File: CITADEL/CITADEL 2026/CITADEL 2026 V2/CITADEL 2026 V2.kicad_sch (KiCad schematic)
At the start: 71 parts, among them J1 FAERIE CAN BUS, J10 ESC PWR, J11 STEPPER 1, J12 STEPPER 2, J13 SERVO DAUGHTER, J2 CITADEL CAN BUS, J3 FAERIE 12V, J4 CITADEL BATTERY, J5 FAERIE BATTERY, J6 LED STRIP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

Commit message: Removed stepper drivers
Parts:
- removed A1, A2: DRV8825, Module:Pololu_Breakout-16_15.2x20.3mm, symbol Driver_Motor:Pololu_Breakout_DRV8825
- removed J11: STEPPER 1, Connector_Molex:Molex_Mini-Fit_Jr_5566-04A_2x02_P4.20mm_Vertical, symbol Connector:Conn_01x04_Socket
- removed J12: STEPPER 2, Connector_Molex:Molex_Mini-Fit_Jr_5566-04A_2x02_P4.20mm_Vertical, symbol Connector:Conn_01x04_Socket
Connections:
- net STEPPER1_STEP: no longer names the net of U1.J3_8 (MTDO/GPIO40)
- net STEPPER2_STEP: no longer names the net of U1.J3_10 (GPIO38)
- net STEPPER_DIR: no longer names the net of U1.J3_9 (MTCK/GPIO39)
- net STEPPER_EN: no longer names the net of U1.J3_4 (GPIO1)
- net STEPPER_M0: no longer names the net of U1.J3_5 (GPIO2)
- net STEPPER_M1: no longer names the net of U1.J3_6 (MTMS/GPIO42)
- net STEPPER_M2: no longer names the net of U1.J3_7 (MTDI/GPIO41)
- no-connect marks 35 -> 40
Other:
- moved on the sheet: C4, J6, J7, J8, R14, R15, R16, R17, R18, R19, R20, R21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

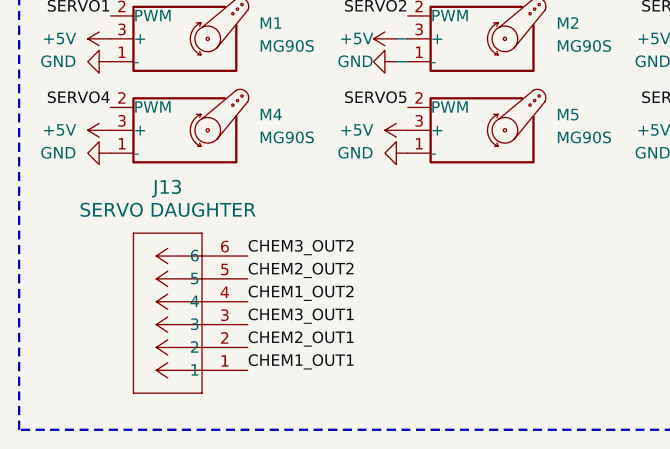
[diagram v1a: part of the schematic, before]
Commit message: Changed linear actuator connectors
Removed the connector for the daughter board and moved the 1x2 molex connectors onto main board
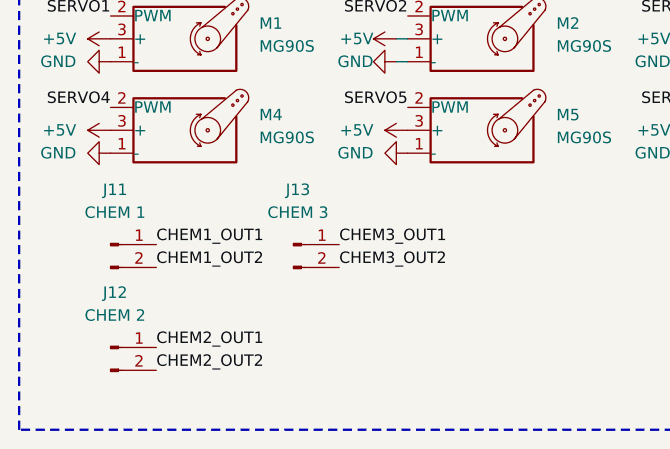
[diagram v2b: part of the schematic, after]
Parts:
- removed J13: SERVO DAUGHTER, Jayse_Footprints:MOLEX_0039281063, symbol 2026-01-24_03-47-07:39281063
- added J11: CHEM 1, Connector_Molex:Molex_Mini-Fit_Jr_5566-02A_2x01_P4.20mm_Vertical, symbol Connector:Conn_01x02_Pin
- added J12: CHEM 2, Connector_Molex:Molex_Mini-Fit_Jr_5566-02A_2x01_P4.20mm_Vertical, symbol Connector:Conn_01x02_Pin
- added J13: CHEM 3, Connector_Molex:Molex_Mini-Fit_Jr_5566-02A_2x01_P4.20mm_Vertical, symbol Connector:Conn_01x02_Pin
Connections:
- net CHEM1_OUT1: now also J11.1 (Pin_1)
- net CHEM1_OUT2: now also J11.2 (Pin_2)
- net CHEM2_OUT1: now also J12.1 (Pin_1)
- net CHEM2_OUT2: now also J12.2 (Pin_2)
- net CHEM3_OUT1: now also J13.1 (Pin_1)
- net CHEM3_OUT2: now also J13.2 (Pin_2)
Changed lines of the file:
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@@
 	)
 	(label "CHEM3_OUT2"
-		(at 43.18 218.44 0)
+		(at 53.34 219.71 0)
 		(effects
 			(font
@@
 	)
 	(label "CHEM3_OUT1"
-		(at 43.18 226.06 0)
+		(at 53.34 217.17 0)
 		(effects
 			(font
@@
 	)
 	(label "CHEM1_OUT2"
-		(at 43.18 223.52 0)
+		(at 33.02 219.71 0)
 		(effects
 			(font
@@
 	)
 	(label "CHEM2_OUT1"
-		(at 43.18 228.6 0)
+		(at 33.02 228.6 0)
 		(effects
 			(font
@@
 	)
 	(label "CHEM1_OUT1"
-		(at 43.18 231.14 0)
+		(at 33.02 217.17 0)
 		(effects
 			(font
@@
 	)
 	(label "CHEM2_OUT2"
-		(at 43.18 220.98 0)
+		(at 33.02 231.14 0)
 		(effects
 			(font
@@
 	)
 	(symbol
+		(lib_id "Connector:Conn_01x02_Pin")
+		(at 27.94 217.17 0)
+		(unit 1)
+		(exclude_from_sim no)
+		(in_bom yes)
+		(on_board yes)
+		(dnp no)
+		(property "Reference" "J11"
+			(at 28.448 211.074 0)
+			(effects
+				(font
+					(size 1.27 1.27)
+				)
+			)
+		)
+		(property "Value" "CHEM 1"
+			(at 28.448 213.614 0)
+			(effects
+				(font
+					(size 1.27 1.27)
+				)
+			)
+		)
+		(property "Footprint" "Connector_Molex:Molex_Mini-Fit_Jr_5566-02A_2x01_P4.20mm_Vertical"
+			(at 27.94 217.17 0)
+			(effects
+				(font
+					(size 1.27 1.27)
+				)
+				(hide yes)
+			)
+		)
+		(property "Datasheet" "~"
+			(at 27.94 217.17 0)
+			(effects
+				(font
+					(size 1.27 1.27)
+				)
+				(hide yes)
+			)
+		)
+		(property "Description" "Generic connector, single row, 01x02, script generated"
+			(at 27.94 217.17 0)
+			(effects
+				(font
+					(size 1.27 1.27)
+				)
+				(hide yes)
+			)
+		)
+		(pin "1"
+		)
+		(pin "2"
+		)
+		(instances
+			(project "CITADEL 2026 V2"
+				(path "/90a2ddca-ec68-4195-87ff-b70a09174bf7"
+					(reference "J11")
+					(unit 1)
+				)
+			)
+		)
+	)
+	(symbol
 		(lib_id "power:GND")
 		(at 93.98 196.85 270)
@@
 	)
 	(symbol
-		(lib_id "2026-01-24_03-47-07:39281063")
-		(at 43.18 231.14 180)
-		(unit 1)
-		(exclude_from_sim no)
-		(in_bom yes)
-		(on_board yes)
-		(dnp no)
-		(fields_autoplaced yes)
-		(property "Reference" "J13"
-			(at 34.29 210.82 0)
-			(effects
-				(font
-					(size 1.524 1.524)
-				)
-			)
-		)
-		(property "Value" "SERVO DAUGHTER"
-			(at 34.29 213.36 0)
-			(effects
-				(font
-					(size 1.524 1.524)
-				)
-			)
-		)
-		(property "Footprint" "Jayse_Footprints:MOLEX_0039281063"
-			(at 43.18 231.14 0)
-			(effects
-				(font
-					(size 1.27 1.27)
-					(italic yes)
-				)
-				(hide yes)
-			)
-		)
-		(property "Datasheet" "https://www.molex.com/en-us/products/part-detail-pdf/39281063?display=pdf"
-			(at 43.18 231.14 0)
-			(effects
-				(font
-					(size 1.27 1.27)
-					(italic yes)
-				)
-				(hide yes)
-			)
-		)
-		(property "Description" ""
-			(at 43.18 231.14 0)
-			(effects
-				(font
-					(size 1.27 1.27)
-				)
-				(hide yes)
-			)
-		)
-		(pin "5"
-		)
-		(pin "4"
-		)
-		(pin "6"
-		)
-		(pin "2"
-		)
-		(pin "1"
-		)
-		(pin "3"
-		)
-		(instances
-			(project "CITADEL 2026 V2"
-				(path "/90a2ddca-ec68-4195-87ff-b70a09174bf7"
-					(reference "J13")
-					(unit 1)
-				)
-			)
-		)
-	)
-	(symbol
 		(lib_id "Connector:Conn_01x02_Pin")
 		(at 142.24 104.14 180)
@@
 	)
 	(symbol
+		(lib_id "Connector:Conn_01x02_Pin")
+		(at 27.94 228.6 0)
+		(unit 1)
+		(exclude_from_sim no)
+		(in_bom yes)
+		(on_board yes)
+		(dnp no)
+		(property "Reference" "J12"
+			(at 28.448 222.504 0)
+			(effects
+				(font
+					(size 1.27 1.27)
+				)
+			)
+		)
+		(property "Value" "CHEM 2"
+			(at 28.448 225.044 0)
+			(effects
+				(font
+					(size 1.27 1.27)
+				)
+			)
+		)
+		(property "Footprint" "Connector_Molex:Molex_Mini-Fit_Jr_5566-02A_2x01_P4.20mm_Vertical"
+			(at 27.94 228.6 0)
+			(effects
+				(font
+					(size 1.27 1.27)
+				)
+				(hide yes)
+			)
+		)
+		(property "Datasheet" "~"
+			(at 27.94 228.6 0)
+			(effects
+				(font
+					(size 1.27 1.27)
+				)
+				(hide yes)
+			)
+		)
+		(property "Description" "Generic connector, single row, 01x02, script generated"
+			(at 27.94 228.6 0)
+			(effects
+				(font
+					(size 1.27 1.27)
+				)
+				(hide yes)
+			)
+		)
+		(pin "1"
+		)
+		(pin "2"
+		)
+		(instances
+			(project "CITADEL 2026 V2"
+				(path "/90a2ddca-ec68-4195-87ff-b70a09174bf7"
+					(reference "J12")
+					(unit 1)
+				)
+			)
+		)
+	)
+	(symbol
 		(lib_id "power:GND")
 		(at 243.84 30.48 0)
@@
 					(unit 1)
 				)
+			)
+		)
+	)
+	(symbol
+		(lib_id "Connector:Conn_01x02_Pin")
+		(at 48.26 217.17 0)
+		(unit 1)
+		(exclude_from_sim no)
+		(in_bom yes)
+		(on_board yes)
+		(dnp no)
+		(property "Reference" "J13"
+			(at 48.768 211.074 0)
+			(effects
+				(font
+					(size 1.27 1.27)
+				)
+			)
+		)
+		(property "Value" "CHEM 3"
+			(at 48.768 213.614 0)
+			(effects
+				(font
+					(size 1.27 1.27)
+				)
+			)
+		)
+		(property "Footprint" "Connector_Molex:Molex_Mini-Fit_Jr_5566-02A_2x01_P4.20mm_Vertical"
+			(at 48.26 217.17 0)
+			(effects
+				(font
+					(size 1.27 1.27)
+				)
+				(hide yes)
+			)
+		)
+		(property "Datasheet" "~"
+			(at 48.26 217.17 0)
+			(effects
+				(font
+					(size 1.27 1.27)
+				)
+				(hide yes)
+			)
+		)
+		(property "Description" "Generic connector, single row, 01x02, script generated"
+			(at 48.26 217.17 0)
+			(effects
+				(font
+					(size 1.27 1.27)
+				)
+				(hide yes)
+			)
+		)
+		(pin "1"
+		)
+		(pin "2"
+		)
+		(instances
+			(project "CITADEL 2026 V2"
+				(path "/90a2ddca-ec68-4195-87ff-b70a09174bf7"
+					(reference "J13")
+					(unit 1)
+				)

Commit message: Updated values for CAN resistors and caps
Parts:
- C1: value C -> 0.1 uF
- C2: value C -> 1 uf
- C3: value C -> 4.7 nF
- R3, R4: value R -> 60 Ω
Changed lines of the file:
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@@
 			)
 		)
-		(property "Value" "C"
+		(property "Value" "1 uf"
 			(at 64.008 135.89 90)
 			(effects
@@
 			)
 		)
-		(property "Value" "C"
+		(property "Value" "0.1 uF"
 			(at 38.1 157.4862 0)
 			(effects
@@
 			)
 		)
-		(property "Value" "C"
+		(property "Value" "4.7 nF"
 			(at 105.918 148.59 90)
 			(effects
@@
 			)
 		)
-		(property "Value" "R"
+		(property "Value" "60 Ω"
 			(at 91.44 143.51 90)
 			(effects
@@
 			)
 		)
-		(property "Value" "R"
+		(property "Value" "60 Ω"
 			(at 91.44 161.544 90)
 			(effects
